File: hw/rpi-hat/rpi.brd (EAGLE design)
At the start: 65 x 56.5 mm, 30 parts, among them U1 BSS138, U2 BSS138, U3 BSS138

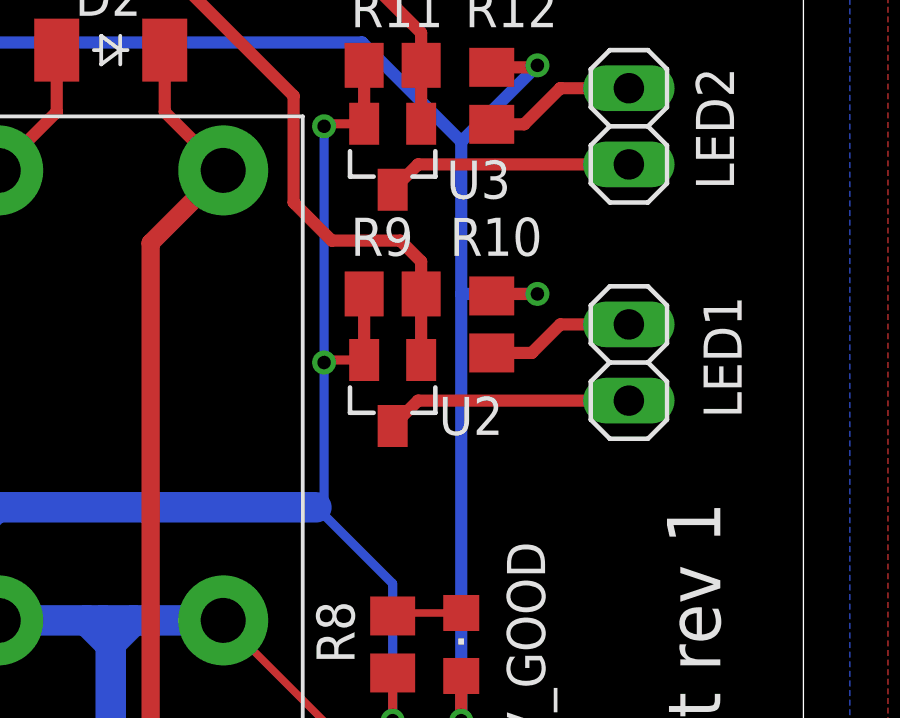
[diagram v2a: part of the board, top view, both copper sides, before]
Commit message: hw/rpi-ha: add bleeder resistors for external LEDs
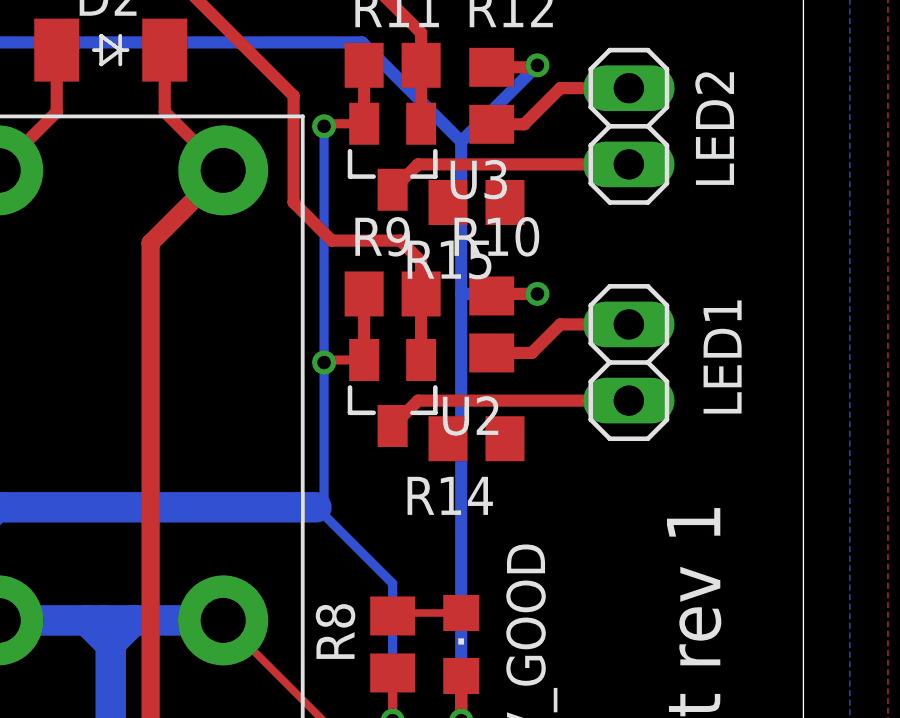
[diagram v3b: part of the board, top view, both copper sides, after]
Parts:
- added R14, R15: 1k, rcl:R0805
- R10, R12: value 150R -> 200R
- R2: value 10k -> 1k
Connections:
- net N$3: now also R14.2
- net N$6: now also R14.1
- net N$7: now also R15.2
- net N$8: now also R15.1
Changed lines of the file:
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@@
 </element>
 <element name="U$2" library="parts" package="JW2FORMC" value="JW2SN-DC12V" x="41.91" y="30.48" smashed="yes" rot="R270"/>
-<element name="R2" library="rcl" library_urn="urn:adsk.eagle:library:334" package="R0805" package3d_urn="urn:adsk.eagle:package:23553/2" value="10k" x="31.8" y="46.662" smashed="yes" rot="R180">
+<element name="R2" library="rcl" library_urn="urn:adsk.eagle:library:334" package="R0805" package3d_urn="urn:adsk.eagle:package:23553/2" value="1k" x="31.8" y="46.662" smashed="yes" rot="R180">
 <attribute name="NAME" x="32.181" y="49.202" size="1.27" layer="25" rot="R180"/>
 <attribute name="POPULARITY" value="86" x="31.8" y="46.662" size="1.778" layer="27" rot="R180" display="off"/>
@@
 <attribute name="VALUE" x="56.007" y="39.116" size="1.27" layer="27" rot="R270"/>
 </element>
-<element name="R10" library="rcl" library_urn="urn:adsk.eagle:library:334" package="R0805" package3d_urn="urn:adsk.eagle:package:23553/2" value="150R" x="54.61" y="37.846" smashed="yes" rot="R270">
+<element name="R10" library="rcl" library_urn="urn:adsk.eagle:library:334" package="R0805" package3d_urn="urn:adsk.eagle:package:23553/2" value="200R" x="54.61" y="37.846" smashed="yes" rot="R270">
 <attribute name="NAME" x="53.213" y="40.132" size="1.27" layer="25"/>
 <attribute name="POPULARITY" value="86" x="54.61" y="37.846" size="1.778" layer="27" rot="R270" display="off"/>
@@
 <attribute name="VALUE" x="56.007" y="46.99" size="1.27" layer="27" rot="R270"/>
 </element>
-<element name="R12" library="rcl" library_urn="urn:adsk.eagle:library:334" package="R0805" package3d_urn="urn:adsk.eagle:package:23553/2" value="150R" x="54.61" y="45.466" smashed="yes" rot="R270">
+<element name="R12" library="rcl" library_urn="urn:adsk.eagle:library:334" package="R0805" package3d_urn="urn:adsk.eagle:package:23553/2" value="200R" x="54.61" y="45.466" smashed="yes" rot="R270">
 <attribute name="NAME" x="53.721" y="47.752" size="1.27" layer="25"/>
 <attribute name="POPULARITY" value="86" x="50.292" y="52.832" size="1.778" layer="27" rot="R270" display="off"/>
 <attribute name="SPICEPREFIX" value="R" x="50.292" y="52.832" size="1.778" layer="27" rot="R270" display="off"/>
+</element>
+<element name="R14" library="rcl" library_urn="urn:adsk.eagle:library:334" package="R0805" package3d_urn="urn:adsk.eagle:package:23553/2" value="1k" x="54.102" y="34.036" smashed="yes" rot="R180">
+<attribute name="NAME" x="54.737" y="32.766" size="1.27" layer="25" rot="R180"/>
+<attribute name="POPULARITY" value="86" x="54.102" y="34.036" size="1.778" layer="27" rot="R180" display="off"/>
+<attribute name="SPICEPREFIX" value="R" x="54.102" y="34.036" size="1.778" layer="27" rot="R180" display="off"/>
+<attribute name="VALUE" x="54.737" y="36.576" size="1.27" layer="27" rot="R180"/>
+</element>
+<element name="R15" library="rcl" library_urn="urn:adsk.eagle:library:334" package="R0805" package3d_urn="urn:adsk.eagle:package:23553/2" value="1k" x="54.102" y="41.91" smashed="yes" rot="R180">
+<attribute name="NAME" x="54.737" y="40.64" size="1.27" layer="25" rot="R180"/>
+<attribute name="POPULARITY" value="86" x="54.102" y="41.91" size="1.778" layer="27" rot="R180" display="off"/>
+<attribute name="SPICEPREFIX" value="R" x="54.102" y="41.91" size="1.778" layer="27" rot="R180" display="off"/>
+<attribute name="VALUE" x="54.737" y="44.45" size="1.27" layer="27" rot="R180"/>
 </element>
 </elements>
@@
 <wire x1="52.154" y1="35.306" x2="51.308" y2="34.46" width="0.4064" layer="1"/>
 <wire x1="59.182" y1="35.306" x2="52.154" y2="35.306" width="0.4064" layer="1"/>
+<contactref element="R14" pad="2"/>
+<wire x1="53.152" y1="34.036" x2="51.308" y2="34.46" width="0" layer="19" extent="1-1"/>
 </signal>
 <signal name="N$6">
@@
 <wire x1="56.896" y1="37.846" x2="59.182" y2="37.846" width="0.4064" layer="1"/>
 <wire x1="55.946" y1="36.896" x2="56.896" y2="37.846" width="0.4064" layer="1"/>
+<contactref element="R14" pad="1"/>
+<wire x1="55.052" y1="34.036" x2="54.61" y2="36.896" width="0" layer="19" extent="1-1"/>
 </signal>
 <signal name="GPIO17">
@@
 <wire x1="51.308" y1="42.334" x2="52.154" y2="43.18" width="0.4064" layer="1"/>
 <wire x1="52.154" y1="43.18" x2="59.182" y2="43.18" width="0.4064" layer="1"/>
+<contactref element="R15" pad="2"/>
+<wire x1="53.152" y1="41.91" x2="51.308" y2="42.334" width="0" layer="19" extent="1-1"/>
 </signal>
 <signal name="N$8">
@@
 <wire x1="55.692" y1="44.516" x2="56.896" y2="45.72" width="0.4064" layer="1"/>
 <wire x1="56.896" y1="45.72" x2="59.182" y2="45.72" width="0.4064" layer="1"/>
+<contactref element="R15" pad="1"/>
+<wire x1="55.052" y1="41.91" x2="54.61" y2="44.516" width="0" layer="19" extent="1-1"/>
 </signal>
 </signals>
